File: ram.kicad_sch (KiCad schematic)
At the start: 54 parts, among them U2 MT41K512M8DA, U5 AS6C8008-55ZIN

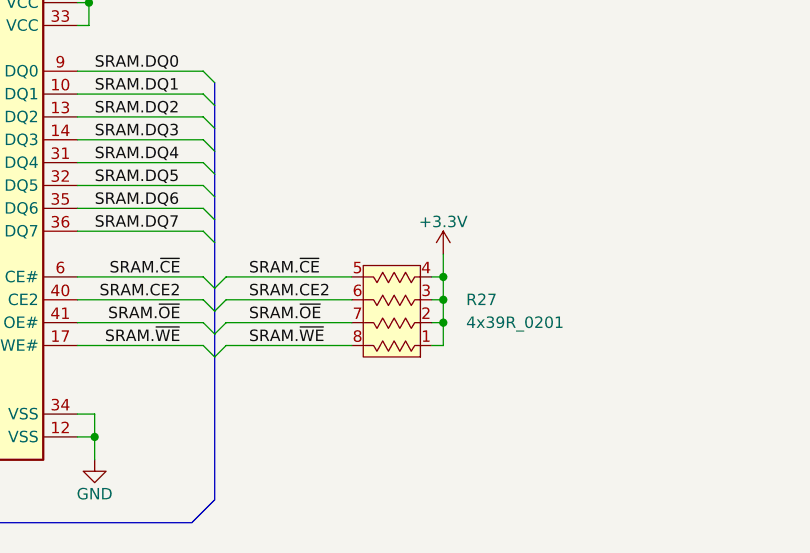
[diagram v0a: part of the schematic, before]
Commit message: Replace resistor ladder with 0402 resistors
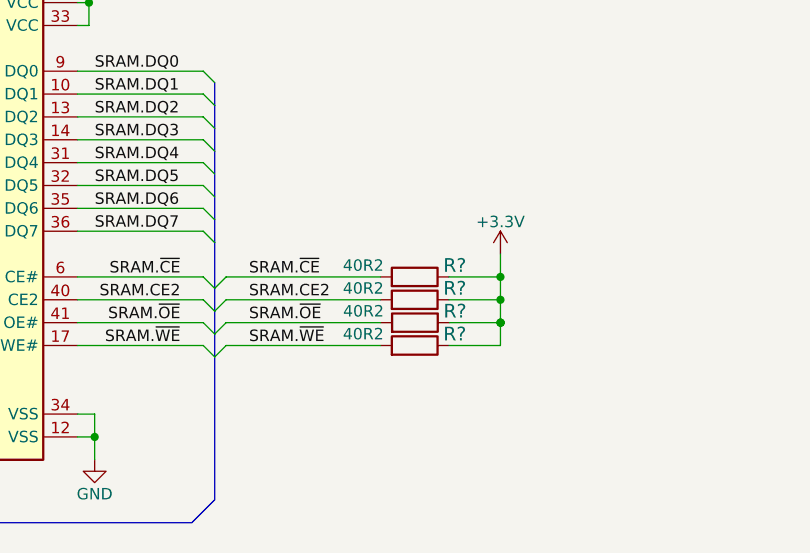
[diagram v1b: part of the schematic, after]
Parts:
- removed R27: 4x39R_0201_array, antmicro-footprints:EXB18V, symbol antmicroResistorNetworksArrays:4x39R_0201_array
- added R? (x4): R_40R2_0201, antmicro-footprints:0201-res, symbol antmicroResistorsmisc:R_40R2_0201
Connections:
- net +3V3: now also R?.1, R?.1, R?.1, R?.1
- net SRAM.CE2: now also R?.2
- net SRAM.~{CE}: now also R?.2
- net SRAM.~{OE}: now also R?.2
- net SRAM.~{WE}: now also R?.2

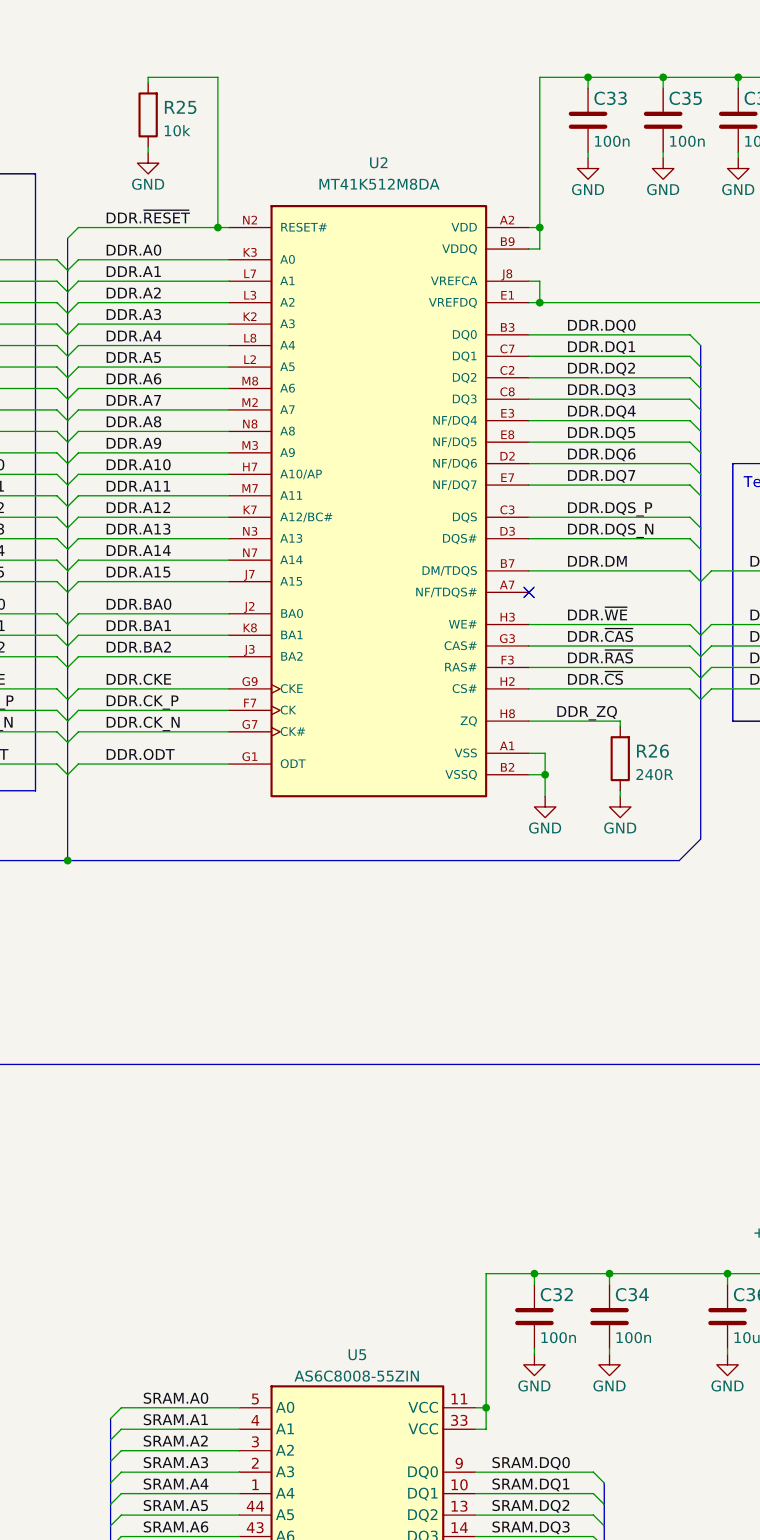
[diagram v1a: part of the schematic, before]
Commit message: Unify reference designator placement
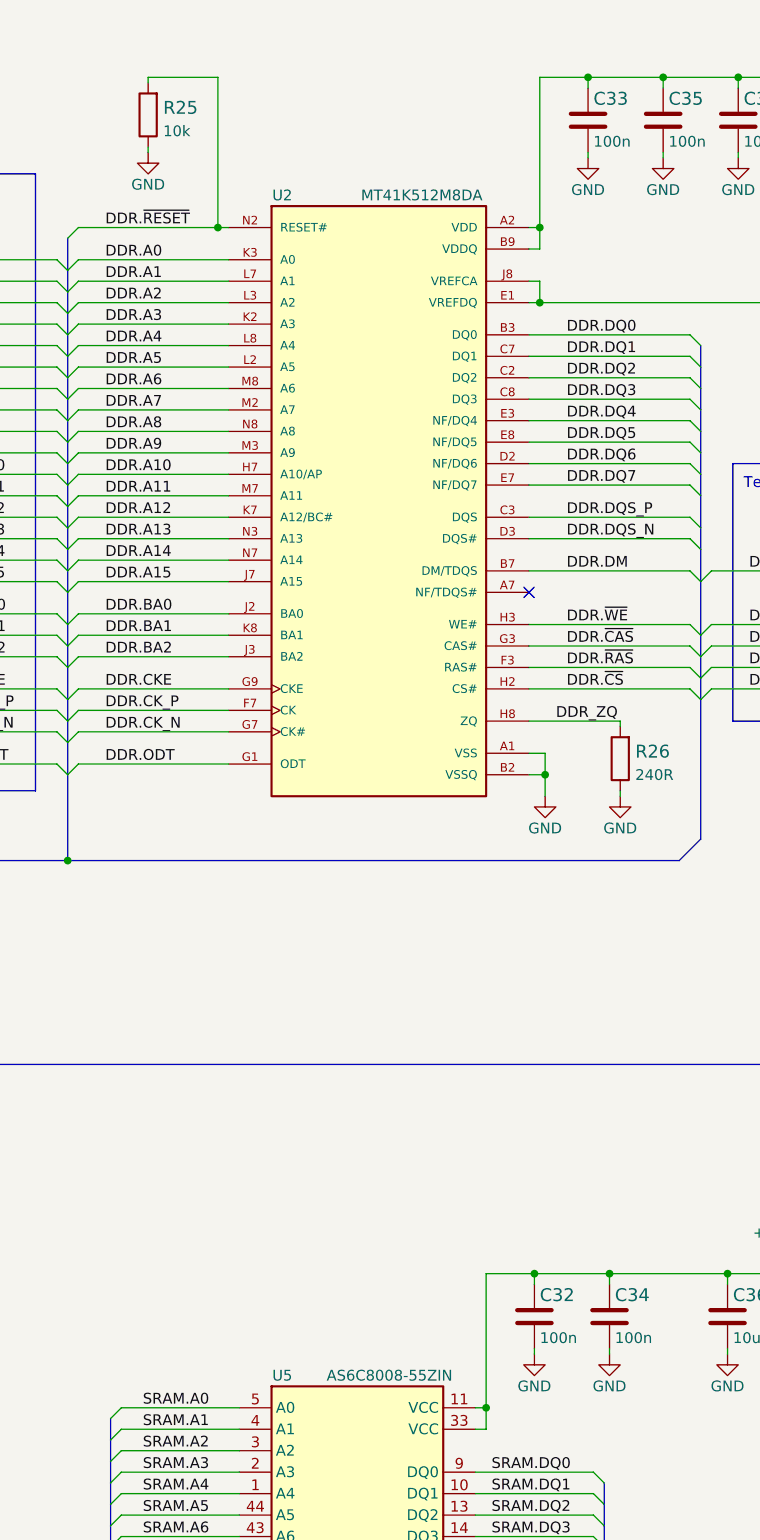
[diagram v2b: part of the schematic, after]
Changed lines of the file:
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@@
   )
   (symbol (lib_id "antmicroMemory:MT41K512M8DA") (at 196.215 81.28 0) (unit 1)
-    (in_bom yes) (on_board yes) (fields_autoplaced)
-    (property "Reference" "U2" (id 0) (at 196.85 39.37 0))
-    (property "Value" "MT41K512M8DA" (id 1) (at 196.85 41.91 0))
+    (in_bom yes) (on_board yes)
+    (property "Reference" "U2" (id 0) (at 185.42 43.18 0))
+    (property "Value" "MT41K512M8DA" (id 1) (at 201.93 43.18 0))
     (property "Footprint" "antmicro-footprints:Micron_FBGA-78" (id 2) (at 196.215 119.38 0)
       (effects (font (size 1.27 1.27)) (justify bottom) hide)
@@
   )
   (symbol (lib_id "antmicroMemory:AS6C8008-55ZIN") (at 194.31 214.63 0) (unit 1)
-    (in_bom yes) (on_board yes) (fields_autoplaced)
-    (property "Reference" "U5" (id 0) (at 194.31 180.4502 0))
-    (property "Value" "AS6C8008-55ZIN" (id 1) (at 194.31 182.9871 0))
+    (in_bom yes) (on_board yes)
+    (property "Reference" "U5" (id 0) (at 185.42 182.88 0))
+    (property "Value" "AS6C8008-55ZIN" (id 1) (at 198.12 182.88 0))
     (property "Footprint" "antmicro-footprints:TSOP-II-44_10.16x18.41mm_P0.8mm" (id 2) (at 194.31 266.7 0)
       (effects (font (size 1.27 1.27)) hide)

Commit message: Add VTT, VREF power buses to RAM
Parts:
- added C? (x2): C_100n_0201, antmicro-footprints:0201-res, symbol antmicroCapacitorsmisc:C_100n_0201
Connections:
- net +0.676_VTT: no longer C44.2, C45.1, C46.2, C47.1, C48.2, C49.1, C50.2, C51.1, C52.2, C53.1, R10.1, R11.1, R12.1, R13.1, R14.1, R15.1, R16.1, R17.1, R18.1, R19.1, R20.1, R21.1, R22.1, R24.1, R3.1, R4.1, R5.1, R6.1, R7.1, R8.1, R9.1
- net GND: now also C?.2, C?.2
- net +0.676_VREF renamed +0V675_VREF
- net +0V675_VREF: now also C?.1, C?.1
- new net +0V675_VTT: C44.2, C45.1, C46.2, C47.1, C48.2, C49.1, C50.2, C51.1, C52.2, C53.1, R10.1, R11.1, R12.1, R13.1, R14.1, R15.1, R16.1, R17.1, R18.1, R19.1, R20.1, R21.1, R22.1, R24.1, R3.1, R4.1, R5.1, R6.1, R7.1, R8.1, R9.1
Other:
- moved on the sheet: C44, C45, C46, C47, C48, C49, C50, C51, C52, C53

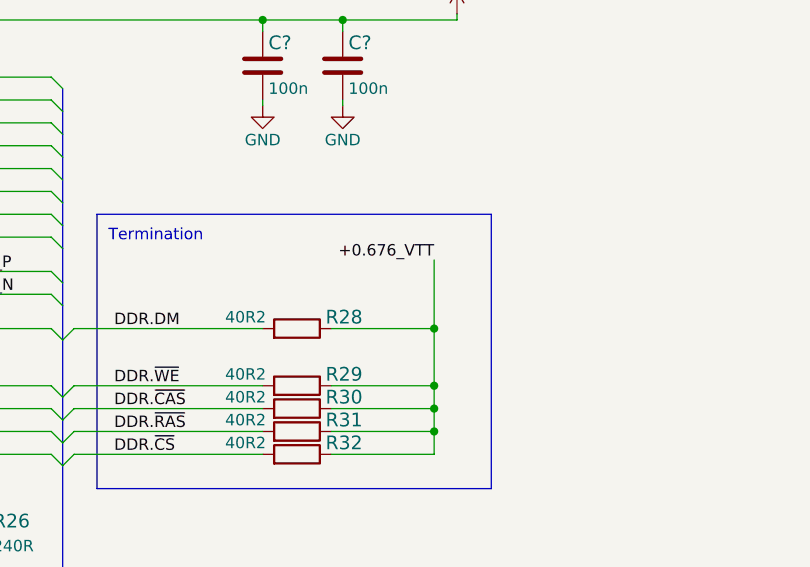
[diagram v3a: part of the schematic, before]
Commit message: Add missing +0V675_VTT power symbol to DDR termination
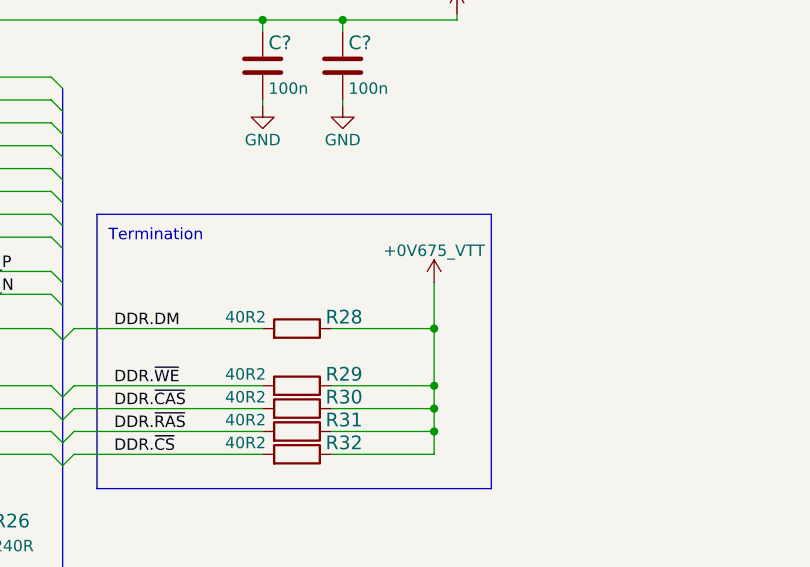
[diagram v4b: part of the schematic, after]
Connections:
- net +0.676_VTT is gone; now on net +0V675_VTT: R28.1, R29.1, R30.1, R31.1, R32.1
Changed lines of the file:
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@@
     (stroke (width 0) (type default) (color 0 0 0 0))
   )
-  (wire (pts (xy 276.225 80.01) (xy 276.225 87.63))
+  (wire (pts (xy 276.225 82.55) (xy 276.225 87.63))
     (stroke (width 0) (type default) (color 0 0 0 0))
   )
@@
   (label "DDR.A7" (at 164.465 68.58 0)
     (effects (font (size 1.27 1.27)) (justify left bottom))
-  )
-  (label "+0.676_VTT" (at 276.225 80.01 180)
-    (effects (font (size 1.27 1.27)) (justify right bottom))
   )
   (label "DDR.DQ3" (at 219.075 67.31 0)
@@
     (pin "9")
   )
+  (symbol (lib_id "antmicroPower:+0V675_VTT") (at 276.225 82.55 0) (unit 1)
+    (in_bom yes) (on_board yes) (fields_autoplaced)
+    (property "Reference" "#PWR?" (id 0) (at 276.225 86.36 0)
+      (effects (font (size 1.27 1.27)) hide)
+    )
+    (property "Value" "+0V675_VTT" (id 1) (at 276.225 78.9742 0))
+    (property "Footprint" "" (id 2) (at 276.225 82.55 0)
+      (effects (font (size 1.27 1.27)) hide)
+    )
+    (property "Datasheet" "" (id 3) (at 276.225 82.55 0)
+      (effects (font (size 1.27 1.27)) hide)
+    )
+    (pin "1")
+  )
   (symbol (lib_id "power:GND") (at 297.815 38.735 0) (unit 1)

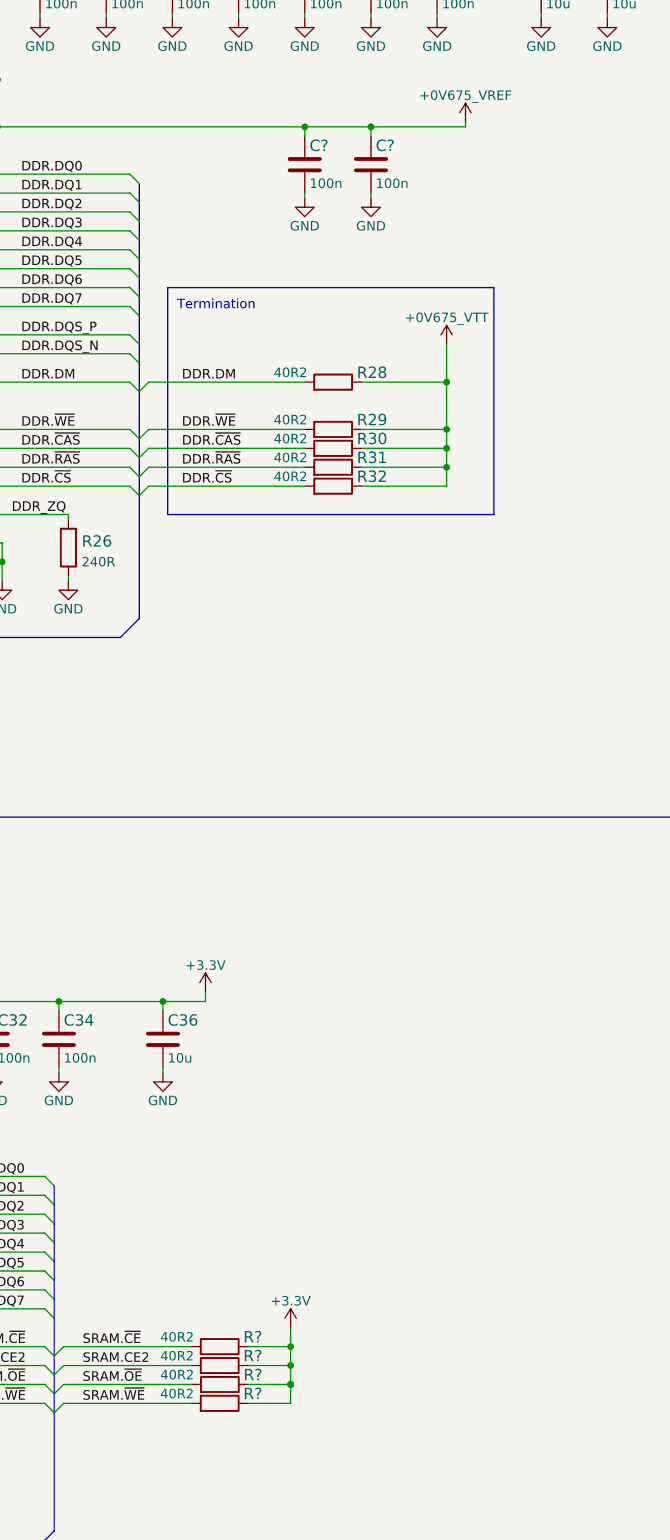
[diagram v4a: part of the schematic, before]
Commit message: Connect MGT supplies, fix FMC+ connector, export components to PCB
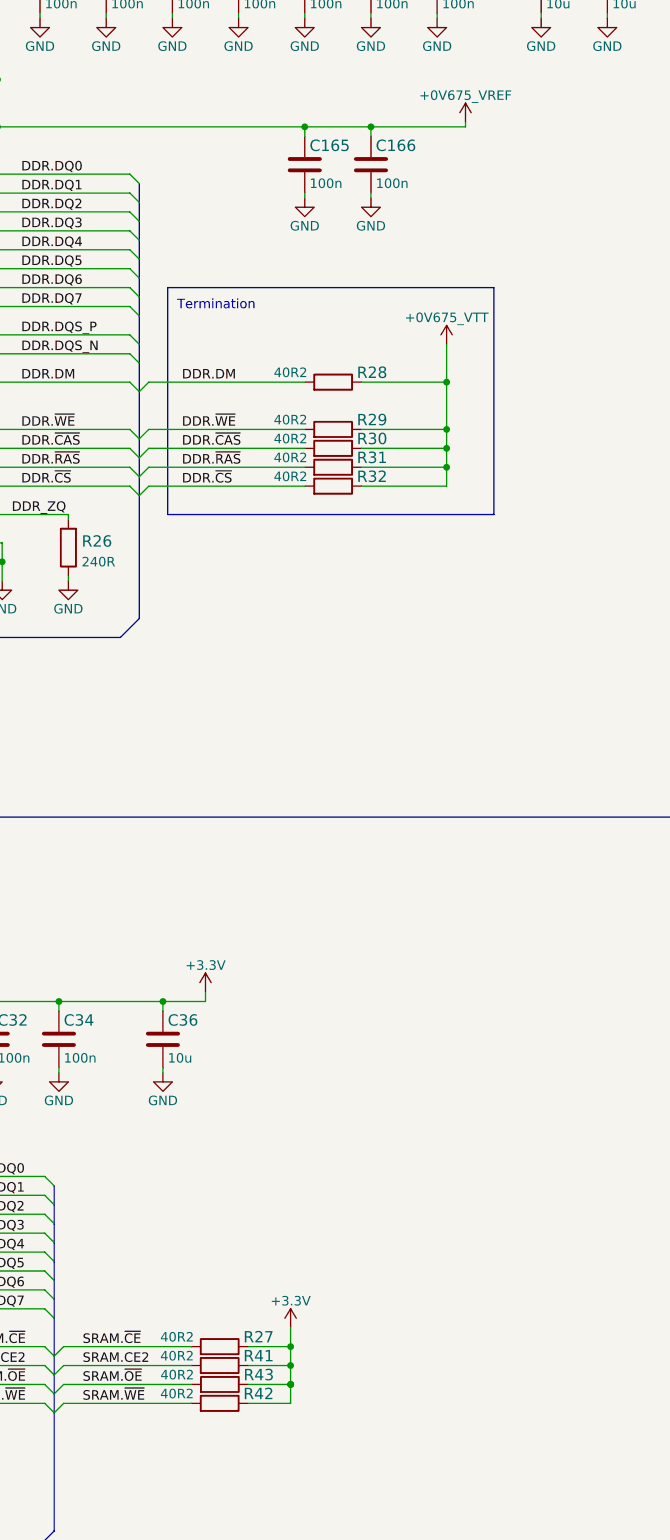
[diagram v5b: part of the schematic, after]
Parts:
- gave numbers to parts that had none: 6
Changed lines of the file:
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@@
   (symbol (lib_id "antmicroPower:+0V675_VTT") (at 118.745 49.53 0) (unit 1)
     (in_bom yes) (on_board yes) (fields_autoplaced)
-    (property "Reference" "#PWR?" (id 0) (at 118.745 53.34 0)
+    (property "Reference" "#PWR0176" (id 0) (at 118.745 53.34 0)
       (effects (font (size 1.27 1.27)) hide)
     )
@@
   (symbol (lib_id "antmicroCapacitorsmisc:C_100n_0201") (at 257.175 58.42 0) (unit 1)
     (in_bom yes) (on_board yes)
-    (property "Reference" "C?" (id 0) (at 257.81 55.88 0)
+    (property "Reference" "C165" (id 0) (at 257.81 55.88 0)
       (effects (font (size 1.524 1.524)) (justify left))
     )
@@
   (symbol (lib_id "antmicroCapacitorsmisc:C_100n_0201") (at 266.065 58.42 0) (unit 1)
     (in_bom yes) (on_board yes)
-    (property "Reference" "C?" (id 0) (at 266.7 55.88 0)
+    (property "Reference" "C166" (id 0) (at 266.7 55.88 0)
       (effects (font (size 1.524 1.524)) (justify left))
     )
@@
   (symbol (lib_id "antmicroResistorsmisc:R_40R2_0201") (at 245.745 217.17 0) (mirror y) (unit 1)
     (in_bom yes) (on_board yes)
-    (property "Reference" "R?" (id 0) (at 248.92 215.9 0)
+    (property "Reference" "R27" (id 0) (at 248.92 215.9 0)
       (effects (font (size 1.524 1.524)) (justify right))
     )
@@
   (symbol (lib_id "antmicroResistorsmisc:R_40R2_0201") (at 245.745 224.79 0) (mirror y) (unit 1)
     (in_bom yes) (on_board yes)
-    (property "Reference" "R?" (id 0) (at 248.92 223.52 0)
+    (property "Reference" "R42" (id 0) (at 248.92 223.52 0)
       (effects (font (size 1.524 1.524)) (justify right))
     )
@@
   (symbol (lib_id "power:GND") (at 257.175 62.865 0) (unit 1)
     (in_bom yes) (on_board yes)
-    (property "Reference" "#PWR?" (id 0) (at 257.175 69.215 0)
+    (property "Reference" "#PWR0174" (id 0) (at 257.175 69.215 0)
       (effects (font (size 1.27 1.27)) hide)
     )
@@
   (symbol (lib_id "antmicroPower:+0V675_VTT") (at 95.25 73.66 0) (unit 1)
     (in_bom yes) (on_board yes) (fields_autoplaced)
-    (property "Reference" "#PWR?" (id 0) (at 95.25 77.47 0)
+    (property "Reference" "#PWR0175" (id 0) (at 95.25 77.47 0)
       (effects (font (size 1.27 1.27)) hide)
     )
@@
   (symbol (lib_id "antmicroResistorsmisc:R_40R2_0201") (at 245.7683 222.25 0) (mirror y) (unit 1)
     (in_bom yes) (on_board yes)
-    (property "Reference" "R?" (id 0) (at 248.9433 220.98 0)
+    (property "Reference" "R43" (id 0) (at 248.9433 220.98 0)
       (effects (font (size 1.524 1.524)) (justify right))
     )
@@
   (symbol (lib_id "antmicroPower:+0V675_VTT") (at 276.225 82.55 0) (unit 1)
     (in_bom yes) (on_board yes) (fields_autoplaced)
-    (property "Reference" "#PWR?" (id 0) (at 276.225 86.36 0)
+    (property "Reference" "#PWR0173" (id 0) (at 276.225 86.36 0)
       (effects (font (size 1.27 1.27)) hide)
     )
@@
   (symbol (lib_id "antmicroPower:+0V675_VREF") (at 278.765 52.705 0) (unit 1)
     (in_bom yes) (on_board yes) (fields_autoplaced)
-    (property "Reference" "#PWR?" (id 0) (at 278.765 56.515 0)
+    (property "Reference" "#PWR0172" (id 0) (at 278.765 56.515 0)
       (effects (font (size 1.27 1.27)) hide)
     )
@@
   (symbol (lib_id "antmicroResistorsmisc:R_40R2_0201") (at 245.745 219.71 0) (mirror y) (unit 1)
     (in_bom yes) (on_board yes)
-    (property "Reference" "R?" (id 0) (at 248.92 218.44 0)
+    (property "Reference" "R41" (id 0) (at 248.92 218.44 0)
       (effects (font (size 1.524 1.524)) (justify right))
     )
@@
   (symbol (lib_id "power:GND") (at 266.065 62.865 0) (unit 1)
     (in_bom yes) (on_board yes)
-    (property "Reference" "#PWR?" (id 0) (at 266.065 69.215 0)
-      (effects (font (size 1.27 1.27)) hide)
-    )
+    (property "Reference" "#PWR0171" (id 0) (at 266.065 69.215 0)
+      (effects (font (size 1.27 1.27)) hide)
+    )

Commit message: Unify designators orientation
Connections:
- net +0V675_VTT: now also R10.2, R11.2, R12.2, R13.2, R14.2, R15.2, R16.2, R17.2, R18.2, R19.2, R20.2, R21.2, R22.2, R24.2, R3.2, R4.2, R5.2, R6.2, R7.2, R8.2, R9.2; no longer R10.1, R11.1, R12.1, R13.1, R14.1, R15.1, R16.1, R17.1, R18.1, R19.1, R20.1, R21.1, R22.1, R24.1, R3.1, R4.1, R5.1, R6.1, R7.1, R8.1, R9.1
- net DDR.A0: now also R3.1; no longer R3.2
- net DDR.A1: now also R4.1; no longer R4.2
- net DDR.A10: now also R13.1; no longer R13.2
- net DDR.A11: now also R14.1; no longer R14.2
- net DDR.A12: now also R15.1; no longer R15.2
- net DDR.A13: now also R16.1; no longer R16.2
- net DDR.A14: now also R17.1; no longer R17.2
- net DDR.A15: now also R18.1; no longer R18.2
- net DDR.A2: now also R5.1; no longer R5.2
- net DDR.A3: now also R6.1; no longer R6.2
- net DDR.A4: now also R7.1; no longer R7.2
- net DDR.A5: now also R8.1; no longer R8.2
- net DDR.A6: now also R9.1; no longer R9.2
- net DDR.A7: now also R10.1; no longer R10.2
- net DDR.A8: now also R11.1; no longer R11.2
- net DDR.A9: now also R12.1; no longer R12.2
- net DDR.BA0: now also R19.1; no longer R19.2
- net DDR.BA1: now also R20.1; no longer R20.2
- net DDR.BA2: now also R21.1; no longer R21.2
- net DDR.CKE: now also R22.1; no longer R22.2
- net DDR.CK_N: now also R23.2; no longer R23.1
- net DDR.CK_P: now also R23.1; no longer R23.2
- net DDR.ODT: now also R24.1; no longer R24.2
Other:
- moved on the sheet: R23
